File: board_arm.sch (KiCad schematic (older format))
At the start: 152 parts, among them SW1 SW_SPDT, U1 STM32F072CBT6, U2 PRTR5V0U2X, U3 MCP1725-3302E_SN

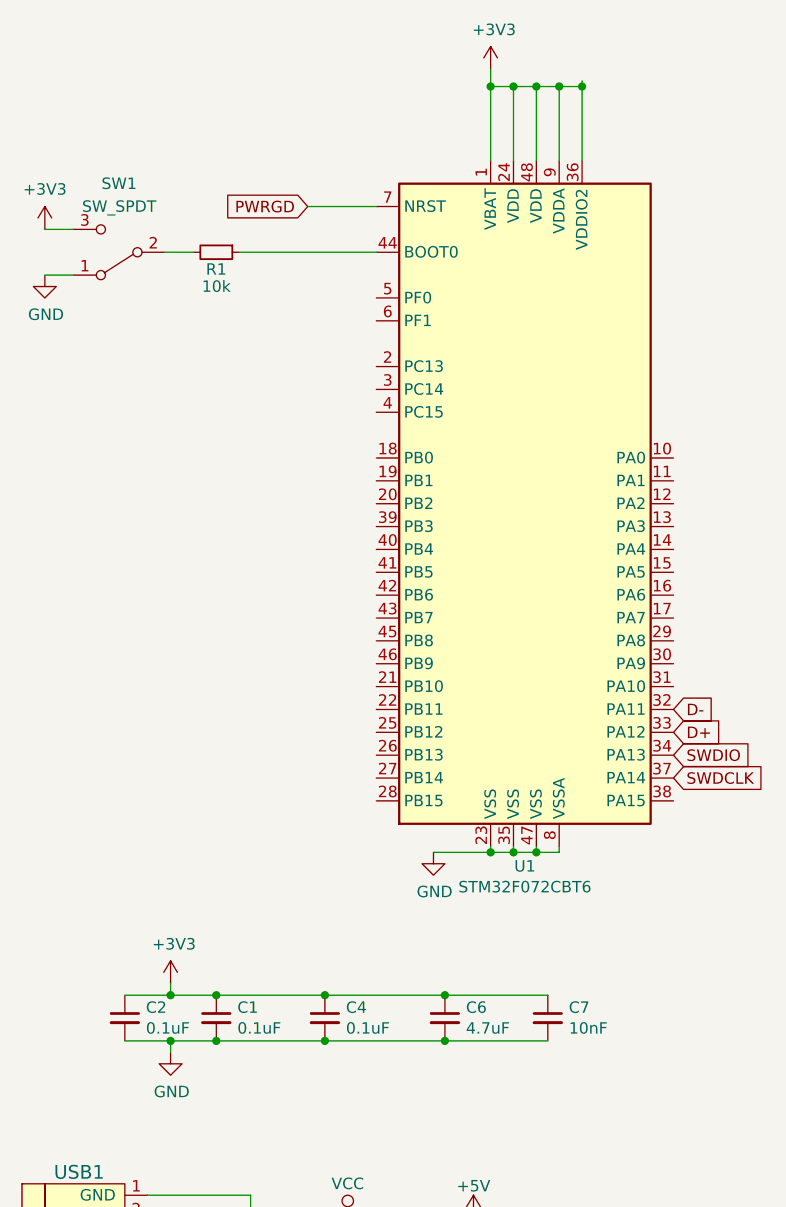
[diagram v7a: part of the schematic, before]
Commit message: Add reset cap
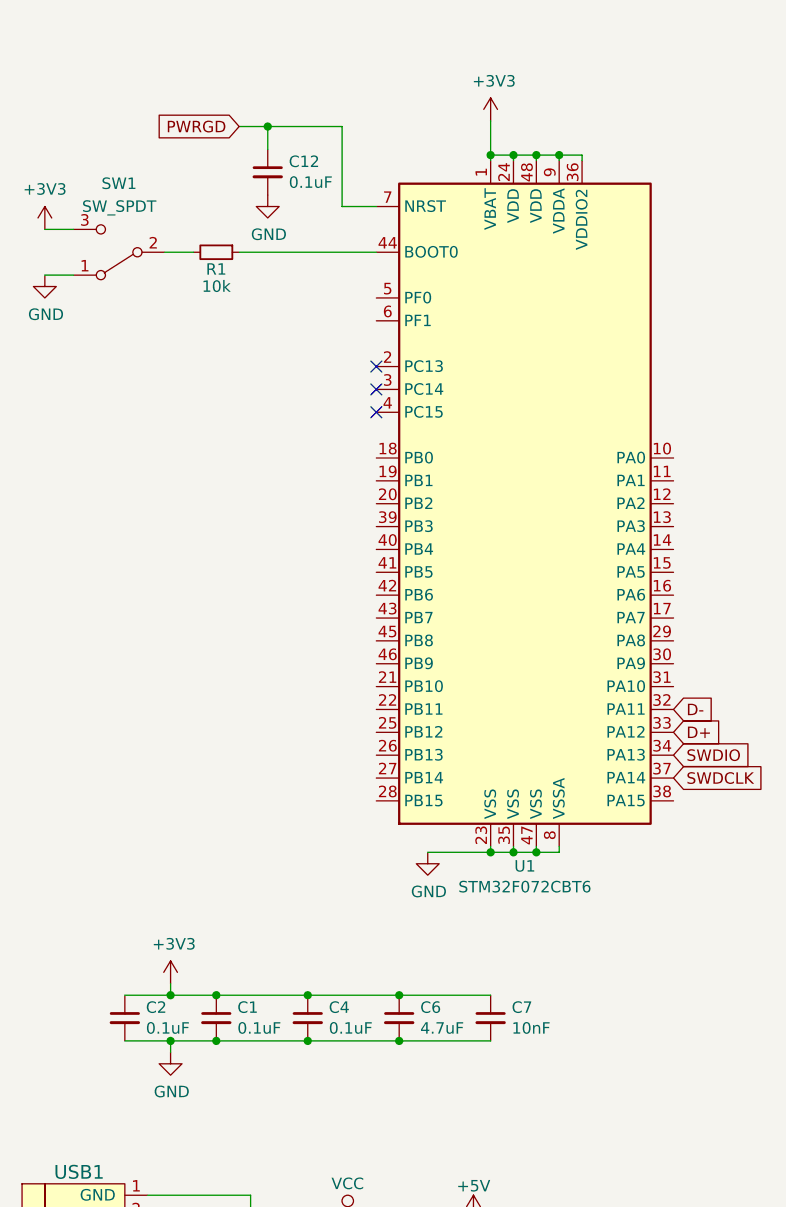
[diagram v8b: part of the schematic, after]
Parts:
- added C12: 0.1uF, Capacitor_SMD:C_0805_2012Metric, symbol Device:C_Small
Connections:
- net GND: now also C12.2
- net PWRGD: now also C12.1
- no-connect marks 0 -> 3
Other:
- moved on the sheet: C4, C6, C7
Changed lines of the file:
@@
 L Device:C_Small C4
 U 1 1 5C605212
-P 2200 5275
-F 0 "C4" H 2292 5321 50  0000 L CNN
-F 1 "0.1uF" H 2292 5230 50  0000 L CNN
-F 2 "Capacitor_SMD:C_0805_2012Metric" H 2200 5275 50  0001 C CNN
-F 3 "~" H 2200 5275 50  0001 C CNN
-	1    2200 5275
+P 2125 5275
+F 0 "C4" H 2217 5321 50  0000 L CNN
+F 1 "0.1uF" H 2217 5230 50  0000 L CNN
+F 2 "Capacitor_SMD:C_0805_2012Metric" H 2125 5275 50  0001 C CNN
+F 3 "~" H 2125 5275 50  0001 C CNN
+	1    2125 5275
 	1    0    0    -1
 $EndComp
@@
 Text GLabel 3725 4225 2    50   Input ~ 0
 SWDCLK
-Text GLabel 2125 1725 0    50   Input ~ 0
+Text GLabel 1825 1375 0    50   Input ~ 0
 PWRGD
 $Comp
 L Device:C_Small C6
 U 1 1 5D2621C9
-P 2725 5275
-F 0 "C6" H 2817 5321 50  0000 L CNN
-F 1 "4.7uF" H 2817 5230 50  0000 L CNN
-F 2 "Capacitor_SMD:C_0805_2012Metric" H 2725 5275 50  0001 C CNN
-F 3 "~" H 2725 5275 50  0001 C CNN
-	1    2725 5275
+P 2525 5275
+F 0 "C6" H 2617 5321 50  0000 L CNN
+F 1 "4.7uF" H 2617 5230 50  0000 L CNN
+F 2 "Capacitor_SMD:C_0805_2012Metric" H 2525 5275 50  0001 C CNN
+F 3 "~" H 2525 5275 50  0001 C CNN
+	1    2525 5275
 	1    0    0    -1
 $EndComp
@@
 L Device:C_Small C7
 U 1 1 5D29FD29
-P 3175 5275
-F 0 "C7" H 3267 5321 50  0000 L CNN
-F 1 "10nF" H 3267 5230 50  0000 L CNN
-F 2 "Capacitor_SMD:C_0805_2012Metric" H 3175 5275 50  0001 C CNN
-F 3 "~" H 3175 5275 50  0001 C CNN
-	1    3175 5275
+P 2925 5275
+F 0 "C7" H 3017 5321 50  0000 L CNN
+F 1 "10nF" H 3017 5230 50  0000 L CNN
+F 2 "Capacitor_SMD:C_0805_2012Metric" H 2925 5275 50  0001 C CNN
+F 3 "~" H 2925 5275 50  0001 C CNN
+	1    2925 5275
 	1    0    0    -1
 $EndComp
@@
 Connection ~ 7150 6600
 Wire Wire Line
-	2125 1725 2425 1725
-Wire Wire Line
 	13975 2050 13975 4775
 Wire Wire Line
@@
 $EndComp
 Wire Wire Line
-	2200 5175 1725 5175
-Connection ~ 2200 5175
-Wire Wire Line
-	1725 5375 2200 5375
-Connection ~ 2200 5375
-Wire Wire Line
-	2925 1125 2925 1200
+	1725 5375 2125 5375
 $Comp
 L power:+3V3 #PWR0101
 U 1 1 5CC8408D
-P 2925 1125
-F 0 "#PWR0101" H 2925 975 50  0001 C CNN
-F 1 "+3V3" H 2940 1298 50  0000 C CNN
-F 2 "" H 2925 1125 50  0001 C CNN
-F 3 "" H 2925 1125 50  0001 C CNN
-	1    2925 1125
-	1    0    0    -1
-$EndComp
-Wire Wire Line
-	2675 4550 2925 4550
+P 2925 1350
+F 0 "#PWR0101" H 2925 1200 50  0001 C CNN
+F 1 "+3V3" H 2940 1523 50  0000 C CNN
+F 2 "" H 2925 1350 50  0001 C CNN
+F 3 "" H 2925 1350 50  0001 C CNN
+	1    2925 1350
+	1    0    0    -1
+$EndComp
 Connection ~ 2925 4550
 $Comp
@@
 	1325 5375 1525 5375
 Connection ~ 1725 5375
-Wire Wire Line
-	3025 1200 3125 1200
-Wire Wire Line
-	3325 1200 3325 1525
-Wire Wire Line
-	3025 1200 3025 1525
-Wire Wire Line
-	3125 1525 3125 1200
-Connection ~ 3125 1200
-Wire Wire Line
-	3125 1200 3225 1200
-Wire Wire Line
-	3325 1200 3325 1175
-Connection ~ 3325 1200
 $Comp
 L power:+3V3 #PWR0104
@@
 	1525 5375 1725 5375
 Wire Wire Line
-	2200 5375 2725 5375
-Wire Wire Line
-	2200 5175 2725 5175
-Wire Wire Line
-	2725 5175 3175 5175
-Connection ~ 2725 5175
-Wire Wire Line
-	3175 5375 2725 5375
-Connection ~ 2725 5375
-Wire Wire Line
 	3225 4550 3125 4550
 Connection ~ 3125 4550
-Wire Wire Line
-	3225 1525 3225 1200
-Connection ~ 3225 1200
-Wire Wire Line
-	3225 1200 3325 1200
-Wire Wire Line
-	2925 1200 3025 1200
-Connection ~ 2925 1200
-Wire Wire Line
-	2925 1200 2925 1525
-Connection ~ 3025 1200
 $Comp
 L power:GND #PWR?
 U 1 1 5D08B550
-P 2675 4550
-F 0 "#PWR?" H 2675 4300 50  0001 C CNN
-F 1 "GND" H 2680 4377 50  0000 C CNN
-F 2 "" H 2675 4550 50  0001 C CNN
-F 3 "" H 2675 4550 50  0001 C CNN
-	1    2675 4550
-	1    0    0    -1
-$EndComp
+P 2650 4550
+F 0 "#PWR?" H 2650 4300 50  0001 C CNN
+F 1 "GND" H 2655 4377 50  0000 C CNN
+F 2 "" H 2650 4550 50  0001 C CNN
+F 3 "" H 2650 4550 50  0001 C CNN
+	1    2650 4550
+	1    0    0    -1
+$EndComp
+NoConn ~ 2425 2425
+NoConn ~ 2425 2525
+NoConn ~ 2425 2625
+$Comp
+L Device:C_Small C12
+U 1 1 5C774367
+P 1950 1575
+F 0 "C12" H 2042 1621 50  0000 L CNN
+F 1 "0.1uF" H 2042 1530 50  0000 L CNN
+F 2 "Capacitor_SMD:C_0805_2012Metric" H 1950 1575 50  0001 C CNN
+F 3 "~" H 1950 1575 50  0001 C CNN
+	1    1950 1575
+	1    0    0    -1
+$EndComp
+$Comp
+L power:GND #PWR?
+U 1 1 5C775F80
+P 1950 1675
+F 0 "#PWR?" H 1950 1425 50  0001 C CNN
+F 1 "GND" H 1955 1502 50  0000 C CNN
+F 2 "" H 1950 1675 50  0001 C CNN
+F 3 "" H 1950 1675 50  0001 C CNN
+	1    1950 1675
+	1    0    0    -1
+$EndComp
+Wire Wire Line
+	1825 1375 1950 1375
+Wire Wire Line
+	1950 1475 1950 1375
+Wire Wire Line
+	2275 1725 2275 1375
+Wire Wire Line
+	2275 1725 2425 1725
+Connection ~ 1950 1375
+Wire Wire Line
+	1950 1375 2275 1375
+Connection ~ 2125 5175
+Wire Wire Line
+	2125 5175 1725 5175
+Connection ~ 2125 5375
+Connection ~ 2525 5175
+Connection ~ 2525 5375
+Wire Wire Line
+	2525 5175 2925 5175
+Wire Wire Line
+	2525 5375 2925 5375
+Wire Wire Line
+	2125 5175 2525 5175
+Wire Wire Line
+	2125 5375 2525 5375
+Wire Wire Line
+	2925 1500 3025 1500
+Connection ~ 2925 1500
+Wire Wire Line
+	2925 1500 2925 1525
+Wire Wire Line
+	3325 1500 3325 1525
+Wire Wire Line
+	2925 1350 2925 1500
+Wire Wire Line
+	3025 1525 3025 1500
+Connection ~ 3025 1500
+Wire Wire Line
+	3025 1500 3125 1500
+Wire Wire Line
+	3125 1525 3125 1500
+Connection ~ 3125 1500
+Wire Wire Line
+	3125 1500 3225 1500
+Wire Wire Line
+	3225 1525 3225 1500
+Connection ~ 3225 1500
+Wire Wire Line
+	3225 1500 3325 1500
+Wire Wire Line
+	2650 4550 2925 4550
 $EndSCHEMATC
